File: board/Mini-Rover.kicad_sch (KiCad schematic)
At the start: 9 parts, among them U2 OKI

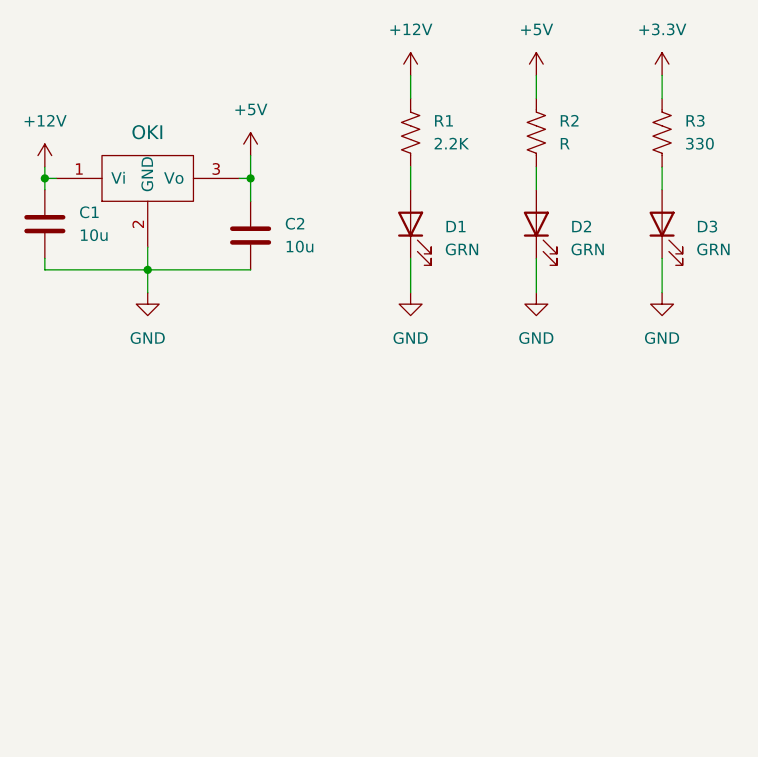
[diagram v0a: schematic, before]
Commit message: Add cell sensing opamp
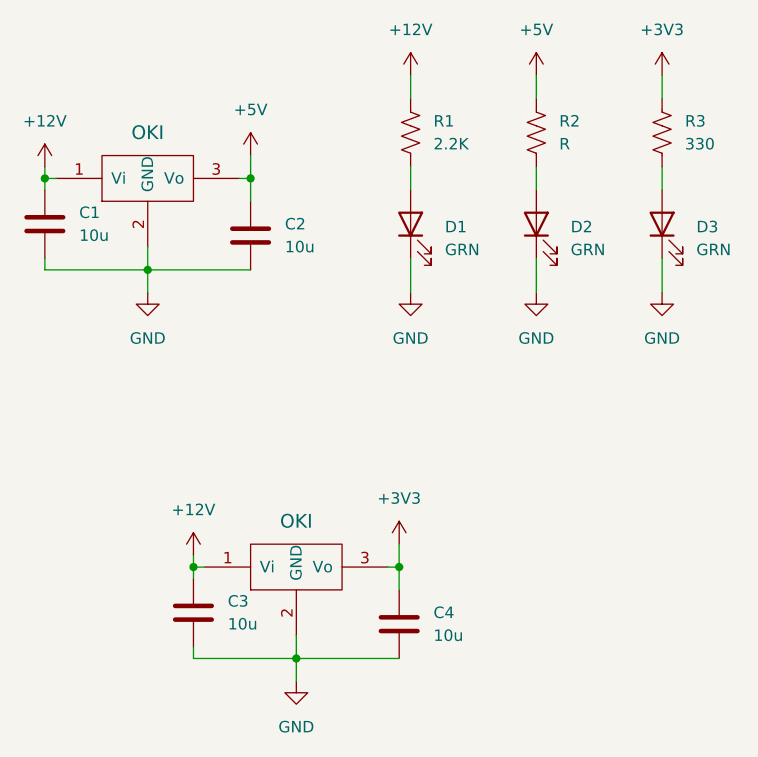
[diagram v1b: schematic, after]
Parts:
- added C3, C4: 10u, symbol Device:C
- added U3: OKI, symbol MRDT_Devices:OKI
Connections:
- net +12V: now also C3.2, U3.1 (Vi)
- net GND: now also C3.1, C4.2, U3.2 (GND)
- net +3.3V renamed +3V3
- net +3V3: now also C4.1, U3.3 (Vo)

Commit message: Add Debbuger
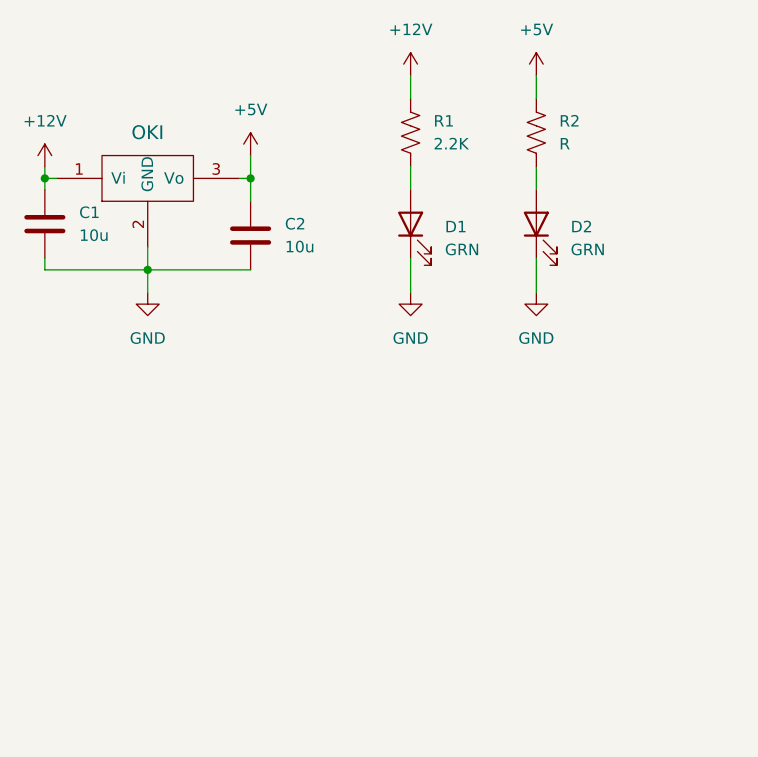
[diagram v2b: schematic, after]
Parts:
- removed C3, C4: 10u, symbol Device:C
- removed D3: GRN, symbol Device:LED
- removed R3: 330, symbol Device:R_US
- removed U3: OKI, symbol MRDT_Devices:OKI

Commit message: fixed some review issues and footprints
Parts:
- C1, C2: value 10u -> 10uF; footprint (none) -> Capacitor_SMD:C_0603_1608Metric_Pad1.08x0.95mm_HandSolder
- D1, D2: footprint (none) -> LED_SMD:LED_0603_1608Metric_Pad1.05x0.95mm_HandSolder
- R1: footprint (none) -> Resistor_SMD:R_0603_1608Metric_Pad0.98x0.95mm_HandSolder
- R2: value R -> 850; footprint (none) -> Resistor_SMD:R_0603_1608Metric_Pad0.98x0.95mm_HandSolder
- U2: footprint (none) -> Converter_DCDC:Converter_DCDC_Murata_OKI-78SR_Horizontal
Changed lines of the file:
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@@
 			)
 		)
-		(property "Footprint" ""
+		(property "Footprint" "LED_SMD:LED_0603_1608Metric_Pad1.05x0.95mm_HandSolder"
 			(at 179.07 46.99 0)
 			(effects
@@
 			)
 		)
-		(property "Footprint" ""
+		(property "Footprint" "Converter_DCDC:Converter_DCDC_Murata_OKI-78SR_Horizontal"
 			(at 125.73 46.99 0)
 			(effects
@@
 			)
 		)
-		(property "Footprint" ""
+		(property "Footprint" "LED_SMD:LED_0603_1608Metric_Pad1.05x0.95mm_HandSolder"
 			(at 165.1 46.99 0)
 			(effects
@@
 			)
 		)
-		(property "Value" "10u"
+		(property "Value" "10uF"
 			(at 128.27 48.2599 0)
 			(effects
@@
 			)
 		)
-		(property "Footprint" ""
+		(property "Footprint" "Capacitor_SMD:C_0603_1608Metric_Pad1.08x0.95mm_HandSolder"
 			(at 123.4948 43.18 0)
 			(effects
@@
 			)
 		)
-		(property "Value" "10u"
+		(property "Value" "10uF"
 			(at 151.13 49.5299 0)
 			(effects
@@
 			)
 		)
-		(property "Footprint" ""
+		(property "Footprint" "Capacitor_SMD:C_0603_1608Metric_Pad1.08x0.95mm_HandSolder"
 			(at 148.2852 52.07 0)
 			(effects
@@
 			)
 		)
-		(property "Value" "R"
+		(property "Value" "850"
 			(at 181.61 38.0999 0)
 			(effects
@@
 			)
 		)
-		(property "Footprint" ""
+		(property "Footprint" "Resistor_SMD:R_0603_1608Metric_Pad0.98x0.95mm_HandSolder"
 			(at 180.086 37.084 90)
 			(effects
@@
 			)
 		)
-		(property "Footprint" ""
+		(property "Footprint" "Resistor_SMD:R_0603_1608Metric_Pad0.98x0.95mm_HandSolder"
 			(at 166.116 37.084 90)
 			(effects

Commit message: Add Layout
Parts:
- U2: footprint Converter_DCDC:Converter_DCDC_Murata_OKI-78SR_Horizontal -> MRDT_Devices:OKI_Horizontal
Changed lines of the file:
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@@
 			)
 		)
-		(property "Footprint" "Converter_DCDC:Converter_DCDC_Murata_OKI-78SR_Horizontal"
+		(property "Footprint" "MRDT_Devices:OKI_Horizontal"
 			(at 125.73 46.99 0)
 			(effects

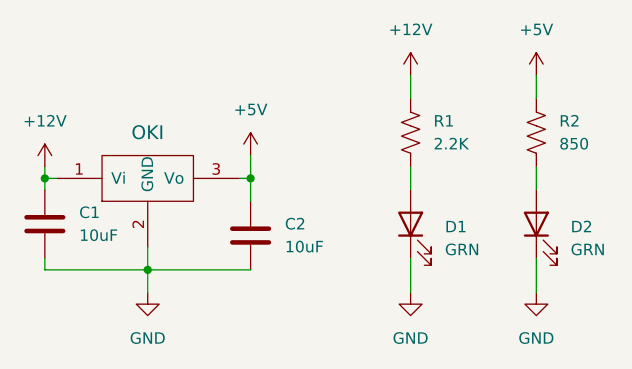
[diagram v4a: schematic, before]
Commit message: Layout started with initial dimensions
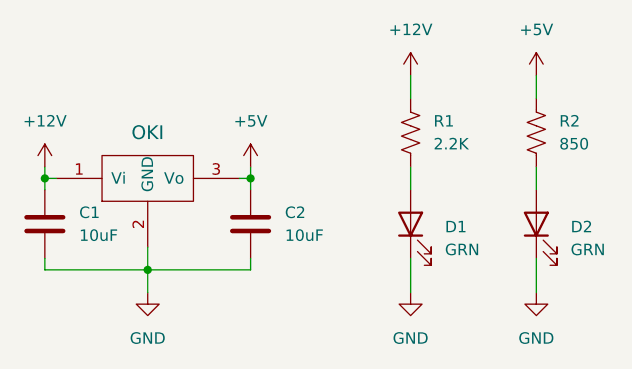
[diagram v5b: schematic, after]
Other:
- moved on the sheet: C2
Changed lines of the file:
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@@
+	(wire
+		(pts
+			(xy 135.89 49.53) (xy 135.89 52.07)
+		)
+		(stroke
+			(width 0)
+			(type default)
+		)
+	)
 	(wire
 		(pts
@@
 	(wire
 		(pts
+			(xy 147.32 52.07) (xy 147.32 50.8)
+		)
+		(stroke
+			(width 0)
+			(type default)
+		)
+	)
+	(wire
+		(pts
 			(xy 179.07 30.48) (xy 179.07 33.02)
 		)
@@
 	(wire
 		(pts
-			(xy 147.32 41.91) (xy 147.32 44.45)
-		)
-		(stroke
-			(width 0)
-			(type default)
-		)
-	)
-	(wire
-		(pts
-			(xy 147.32 39.37) (xy 147.32 41.91)
+			(xy 147.32 41.91) (xy 147.32 43.18)
+		)
+		(stroke
+			(width 0)
+			(type default)
+		)
+	)
+	(wire
+		(pts
+			(xy 147.32 40.64) (xy 147.32 41.91)
 		)
 		(stroke
@@
 		(pts
 			(xy 146.05 41.91) (xy 147.32 41.91)
-		)
-		(stroke
-			(width 0)
-			(type default)
-		)
-	)
-	(wire
-		(pts
-			(xy 135.89 49.53) (xy 135.89 52.07)
 		)
 		(stroke
@@
 	(symbol
 		(lib_id "power:+3.3V")
-		(at 147.32 39.37 0)
+		(at 147.32 40.64 0)
 		(unit 1)
 		(exclude_from_sim no)
@@
 		(fields_autoplaced yes)
 		(property "Reference" "#PWR03"
-			(at 147.32 43.18 0)
+			(at 147.32 44.45 0)
 			(effects
 				(font
@@
 		)
 		(property "Value" "+5V"
-			(at 147.32 34.29 0)
+			(at 147.32 35.56 0)
 			(effects
 				(font
@@
 		)
 		(property "Footprint" ""
-			(at 147.32 39.37 0)
+			(at 147.32 40.64 0)
 			(effects
 				(font
@@
 		)
 		(property "Datasheet" ""
-			(at 147.32 39.37 0)
+			(at 147.32 40.64 0)
 			(effects
 				(font
@@
 		)
 		(property "Description" "Power symbol creates a global label with name \"+3.3V\""
-			(at 147.32 39.37 0)
+			(at 147.32 40.64 0)
 			(effects
 				(font
@@
 	(symbol
 		(lib_id "Device:C")
-		(at 147.32 48.26 0)
+		(at 147.32 46.99 0)
 		(unit 1)
 		(exclude_from_sim no)
@@
 		(fields_autoplaced yes)
 		(property "Reference" "C2"
-			(at 151.13 46.9899 0)
+			(at 151.13 45.7199 0)
 			(effects
 				(font
@@
 		)
 		(property "Value" "10uF"
-			(at 151.13 49.5299 0)
+			(at 151.13 48.2599 0)
 			(effects
 				(font
@@
 		)
 		(property "Footprint" "Capacitor_SMD:C_0603_1608Metric_Pad1.08x0.95mm_HandSolder"
-			(at 148.2852 52.07 0)
+			(at 148.2852 50.8 0)
 			(effects
 				(font
@@
 		)
 		(property "Datasheet" "~"
-			(at 147.32 48.26 0)
+			(at 147.32 46.99 0)
 			(effects
 				(font
@@
 		)
 		(property "Description" "Unpolarized capacitor"
-			(at 147.32 48.26 0)
-			(effects
-				(font
+			(at 147.32 46.99 0)
+			(effects
+				(font
